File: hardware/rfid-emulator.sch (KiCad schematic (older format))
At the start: 99 parts, among them J1 AVR-JTAG-10, J2 Micro_USB, J3 OSTTC020162, Q1 2N3904, Q2 2N3906, Q3 2N3906, Q4 FQP30N06L, Q5 FQP30N06L, SW1 EN11-HSM1BF20, U1 NHD-C0216CiZ-FSW-FBW-3V3, U2 LT8613, U3 ATmega64A-AU, U4 MCP73832-2-OT, U5 LF33_TO252, U6 FT230XS, U7 LM324DT, Y1 ECS-160-20-5PX-TR

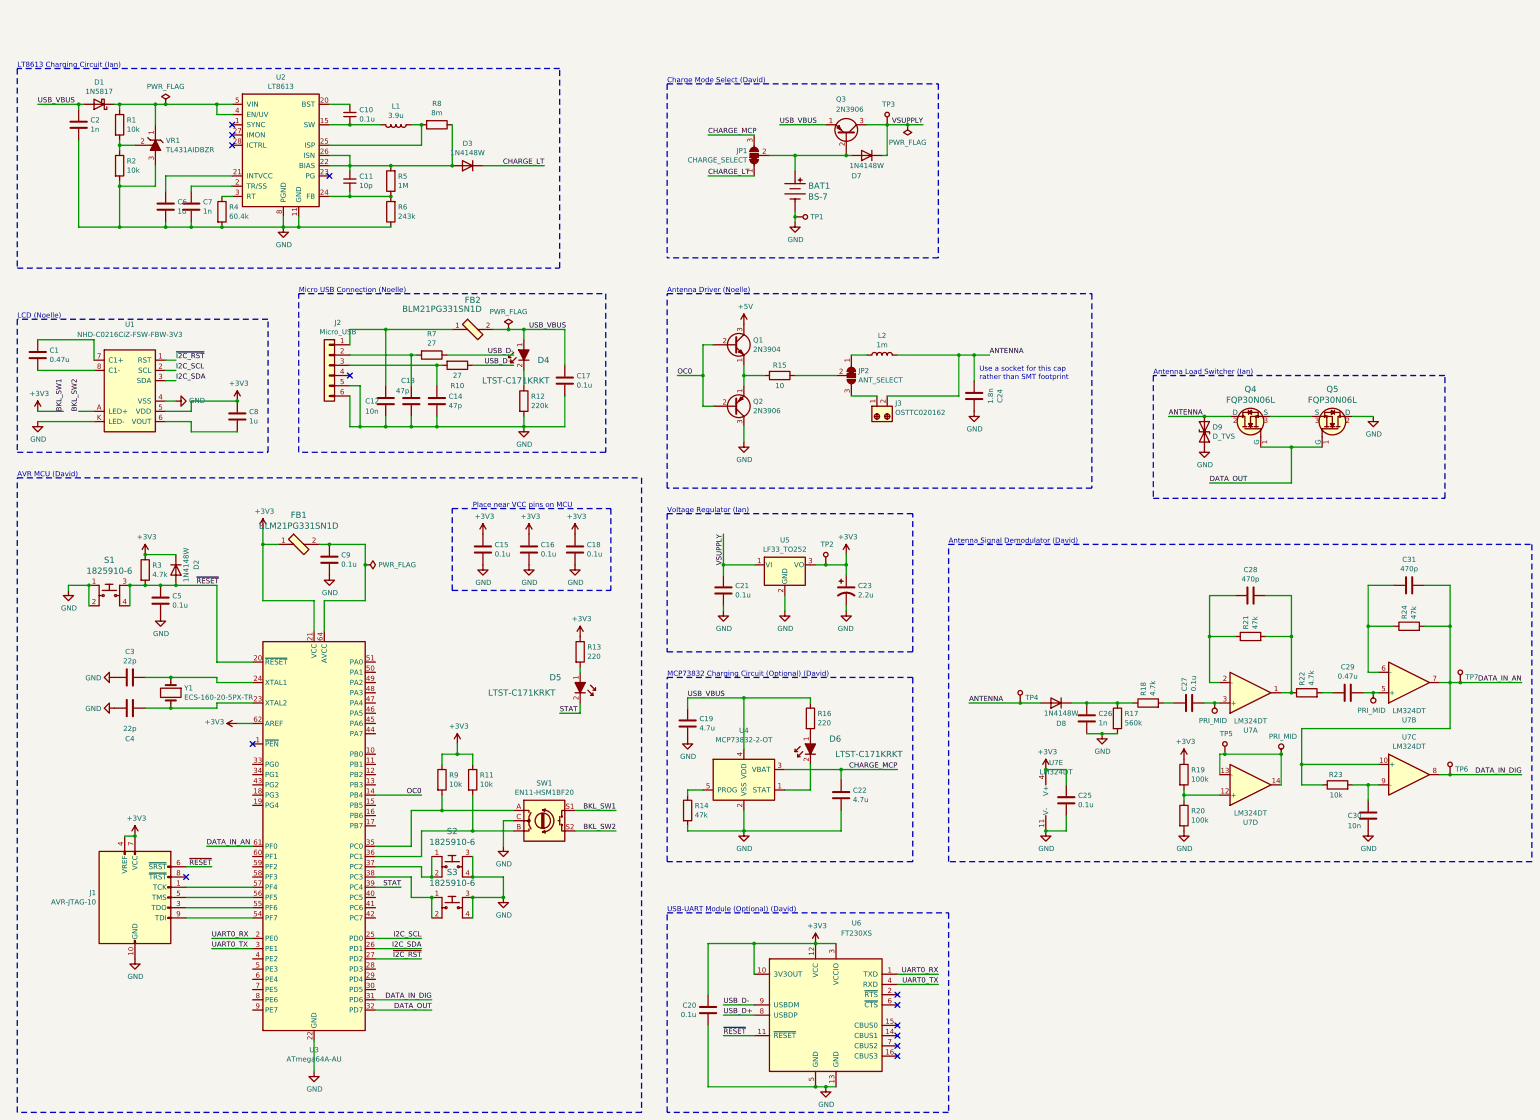
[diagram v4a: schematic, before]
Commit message: Layout for most parts
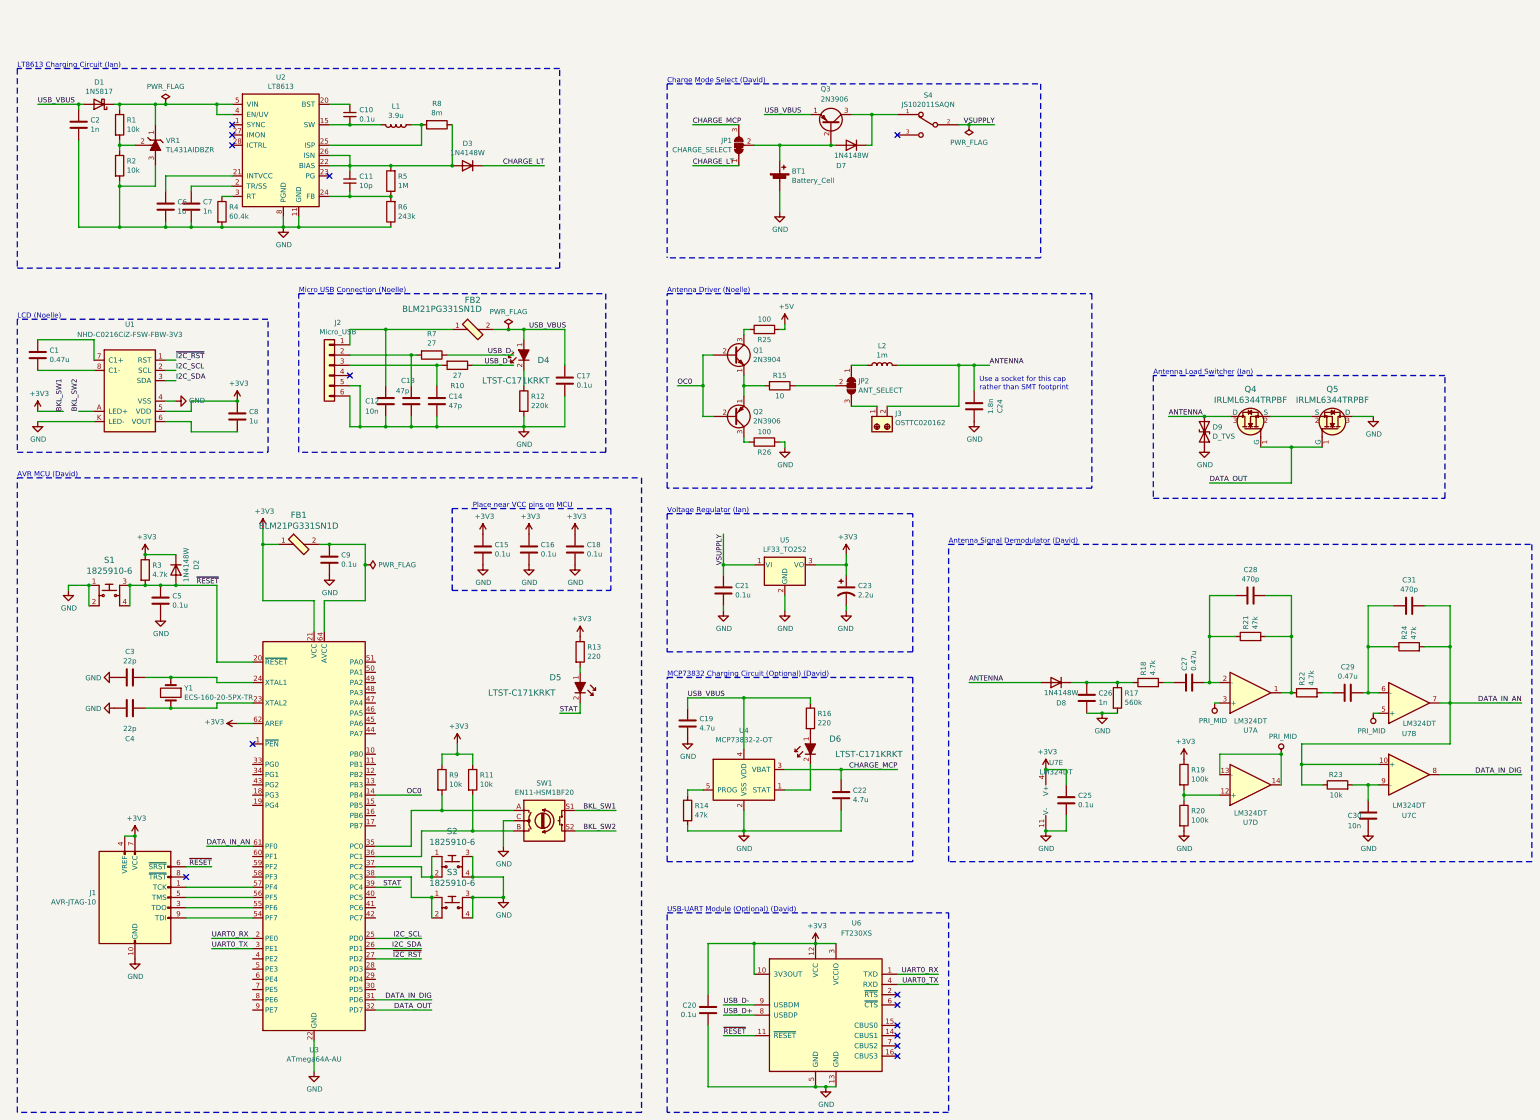
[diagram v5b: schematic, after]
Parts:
- removed BAT1: BS-7, digikey-footprints:Battery_Holder_Coin_2032_BS-7, symbol dk_Battery-Holders-Clips-Contacts:BS-7
- removed Q4, Q5: FQP30N06L, digikey-footprints:TO-220-3, symbol dk_Transistors-FETs-MOSFETs-Single:FQP30N06L
- removed TP1: 5001, digikey-footprints:Test_Point_D1.02mm, symbol dk_Test-Points:5001
- removed TP2, TP3, TP5: 5000, digikey-footprints:Test_Point_D1.02mm, symbol dk_Test-Points:5000
- removed TP4, TP6, TP7: 5002, digikey-footprints:Test_Point_D1.02mm, symbol dk_Test-Points:5002
- added BT1: Battery_Cell, rfid-footprints:KEYSTONE-3034, symbol Device:Battery_Cell
- added Q4, Q5: IRLML6344TRPBF, digikey-footprints:SOT-23-3, symbol dk_Transistors-FETs-MOSFETs-Single:IRLML6344TRPBF
- added R25, R26: 100, Resistors_SMD:R_0805_HandSoldering, symbol Device:R
- added S4: JS102011SAQN, rfid-footprints:SW_JS102011SAQN, symbol rfid-emulator:JS102011SAQN
- C27: value 0.1u -> 0.47u; Part C0805C104Z5VACTU -> (none)
- L1: footprint (none) -> rfid-footprints:CDRH6D28; Part (none) -> CDRH6D28NP-3R9NC
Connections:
- net +5V: now also R25.2; no longer Q1.3 (C)
- net ANTENNA: now also Q4.3 (D)
- net DATA_OUT: now also Q4.1 (G), Q5.1 (G)
- net GND: now also BT1.2 (-), Q5.3 (D), R26.2; no longer Q2.3 (C)
- net PRI_MID: no longer C27.2, C29.1
- net VSUPPLY: now also S4.2; no longer D7.1 (K), Q3.3 (C)
- net at C28.2, R21.1, U7.2 (-): now also C27.2
- net at D7.2 (A), JP1.2 (C), Q3.2 (B): now also BT1.1 (+)
- net at C31.2, R24.1, U7.6 (-): now also C29.1
- new net: Q1.3 (C), R25.1
- new net: Q2.3 (C), R26.1
- new net: D7.1 (K), Q3.3 (C), S4.1
- new net: Q4.2 (S), Q5.2 (S)
- no-connect marks 13 -> 14
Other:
- moved on the sheet: C24, C26, C27, C31, D7, D8, J3, JP1, JP2, L2, Q1, Q2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

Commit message: Re-add Noelle's changes
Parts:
- added C32: 1.5n, Capacitors_SMD:C_0805_HandSoldering, symbol Device:C
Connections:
- net GND: now also C32.1
- net at JP2.2 (C), R15.1: now also C32.2
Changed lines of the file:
@@
 $EndComp
 Wire Wire Line
-	8300 3850 8700 3850
+	8300 3850 8450 3850
 $Comp
 L Device:R R26
@@
 	13250 7350 13250 7550
 Connection ~ 13250 7550
+$Comp
+L Device:C C32
+U 1 1 5DD510A8
+P 8450 4150
+F 0 "C32" V 8198 4150 50  0000 C CNN
+F 1 "1.5n" V 8289 4150 50  0000 C CNN
+F 2 "Capacitors_SMD:C_0805_HandSoldering" H 8488 4000 50  0001 C CNN
+F 3 "~" H 8450 4150 50  0001 C CNN
+	1    8450 4150
+	-1   0    0    1
+$EndComp
+Wire Wire Line
+	8450 4300 8450 4400
+Wire Wire Line
+	8450 4400 8200 4400
+Connection ~ 8200 4400
+Wire Wire Line
+	8450 4000 8450 3850
+Connection ~ 8450 3850
+Wire Wire Line
+	8450 3850 8700 3850
 $EndSCHEMATC

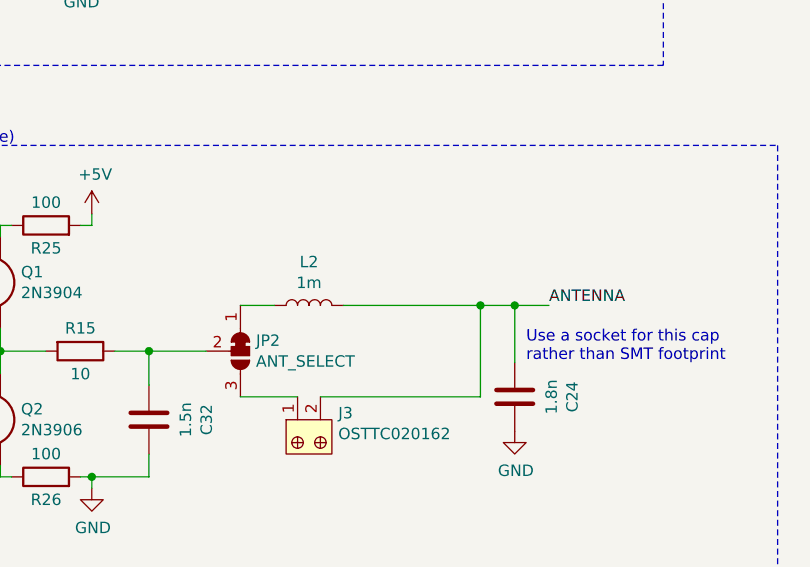
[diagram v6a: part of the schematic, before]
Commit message: Fix most DRC failures on PCB check
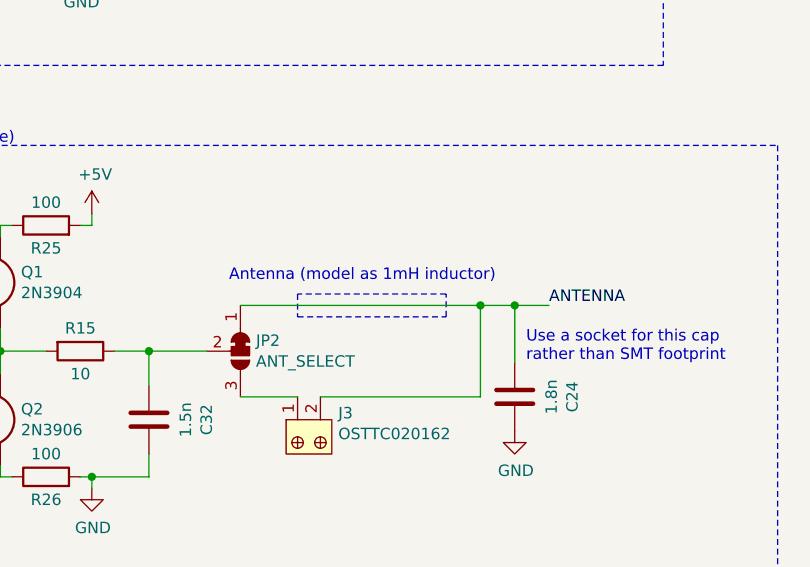
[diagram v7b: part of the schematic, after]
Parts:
- removed L2: 1m, symbol Device:L
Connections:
- net ANTENNA: now also JP2.1 (A)
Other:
- note added: "Antenna (model as 1mH inductor)"
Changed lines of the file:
@@
 	1    0    0    -1
-$EndComp
-$Comp
-L Device:L L2
-U 1 1 5DFFE6EE
-P 9150 3650
-F 0 "L2" V 9340 3650 50  0000 C CNN
-F 1 "1m" V 9249 3650 50  0000 C CNN
-F 2 "" H 9150 3650 50  0001 C CNN
-F 3 "~" H 9150 3650 50  0001 C CNN
-	1    9150 3650
-	0    -1   -1   0
 $EndComp
 Wire Wire Line
@@
 Wire Wire Line
 	12550 4150 12300 4150
-Wire Wire Line
-	8850 3650 9000 3650
 Connection ~ 9900 3650
 Wire Wire Line
@@
 	0    1    1    0
 $EndComp
-Wire Wire Line
-	9300 3650 9900 3650
 Wire Wire Line
 	9200 4050 9900 4050
@@
 Wire Wire Line
 	8450 3850 8700 3850
+Wire Wire Line
+	8850 3650 9900 3650
+Wire Notes Line
+	9100 3600 9100 3700
+Wire Notes Line
+	9100 3700 9750 3700
+Wire Notes Line
+	9750 3700 9750 3600
+Wire Notes Line
+	9750 3600 9100 3600
+Text Notes 8800 3550 0    50   ~ 0
+Antenna (model as 1mH inductor)
 $EndSCHEMATC
